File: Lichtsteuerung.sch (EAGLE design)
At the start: 186 parts, among them IC1 74HC595D, IC10 TSR_1-2450, IC11 MEGA64-A, IC12 75176AD, IC13 DS1307SO8, IC2 74HC595D, IC3 74HC595D, IC4 74HC595D, IC5 75176AD, IC6 MEGA8-AI, IC9 24FC128-I/SN, Q1 32.768, Q2 16MHz, Q3 16MHz, U1 MAX232SOIC16, X1 713-1410, X2 713-1410, X3 733-333, X5 713-1410, X6 733-334, X7 733-333, X8 733-333

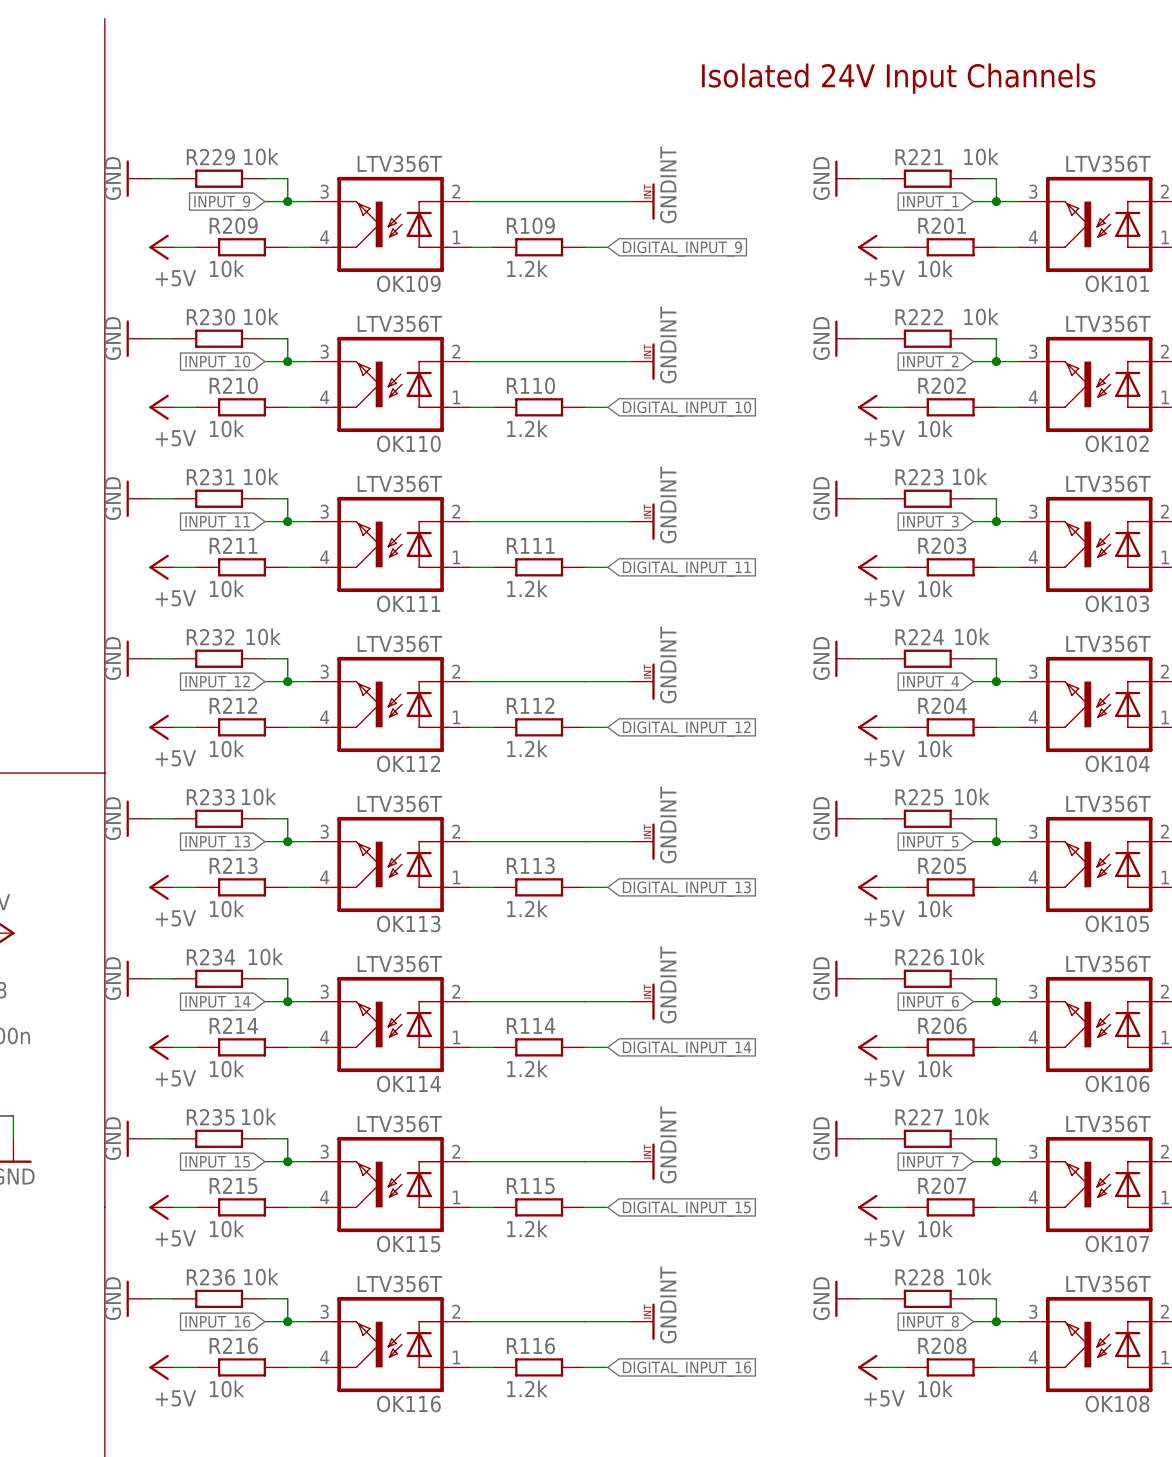
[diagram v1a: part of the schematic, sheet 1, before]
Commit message: Changed pulldown resistors from 10k to 47k for the input optocouplers
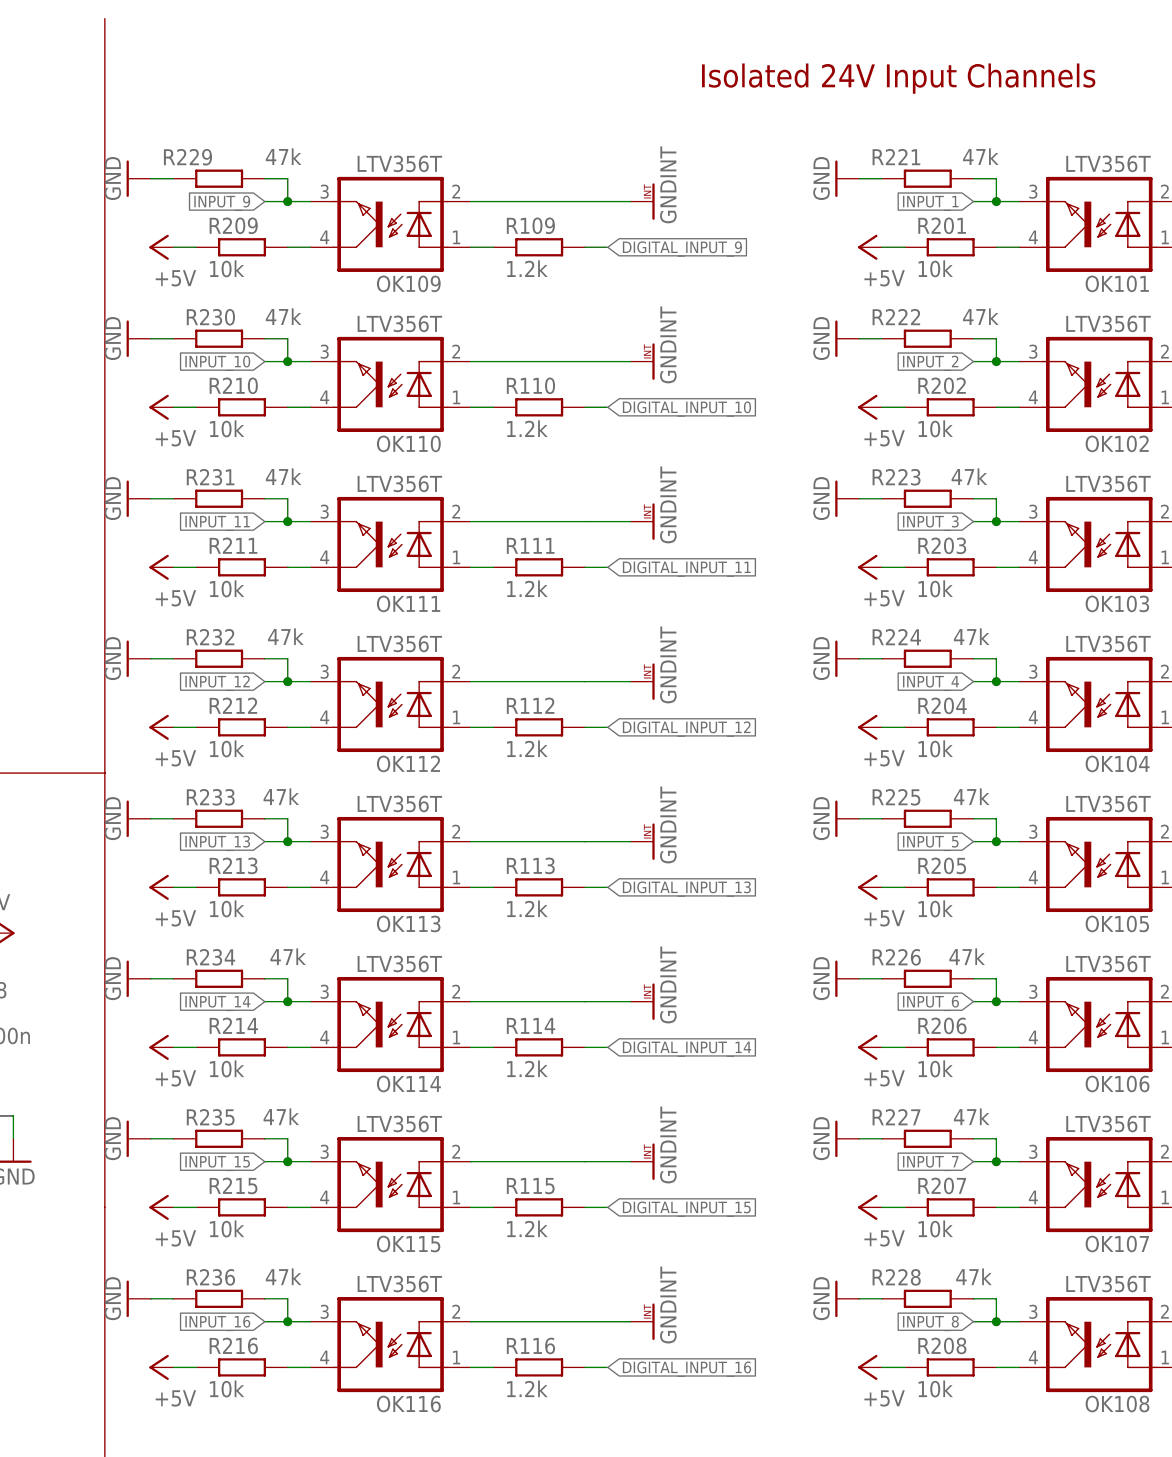
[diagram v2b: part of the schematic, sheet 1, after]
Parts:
- R221, R222, R223, R224, R225, R226, R227, R228, R229, R230, R231, R232, R233, R234, R235, R236: value 10k -> 47k; OC_REICHELT SMD-0805 10,0K -> SMD-0805 47,0K

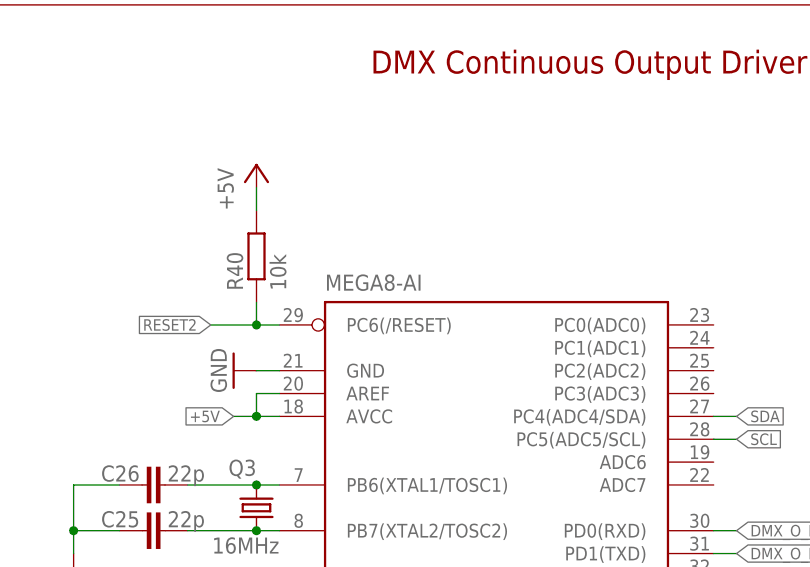
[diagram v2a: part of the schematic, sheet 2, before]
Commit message: Replaced atmega8 with atmega168 in order to use the DMXSerial library
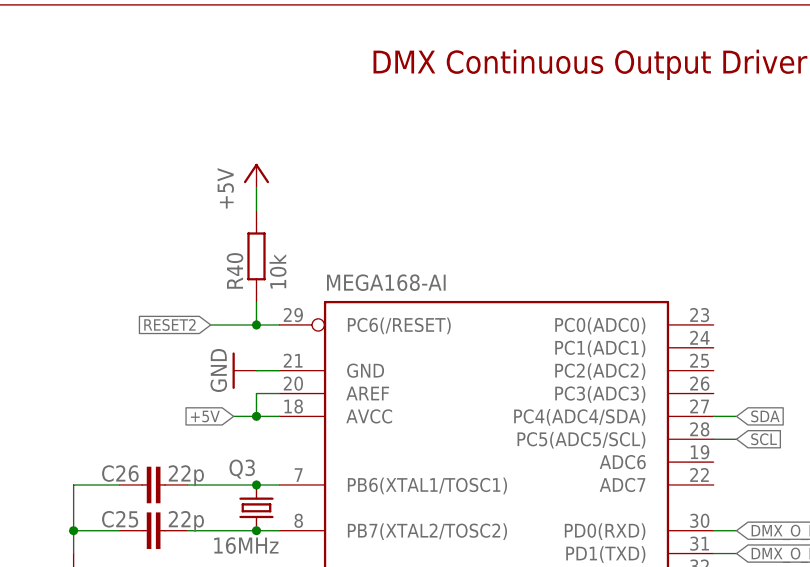
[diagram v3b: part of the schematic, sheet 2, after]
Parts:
- IC6: value MEGA8-AI -> MEGA168-AI; OC_REICHELT ATMEGA 8A-AU -> ATMEGA 168A-AU
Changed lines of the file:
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@@
 <part name="P+17" library="supply1" deviceset="+5V" device=""/>
 <part name="GND29" library="supply1" deviceset="GND" device=""/>
-<part name="IC6" library="atmel" deviceset="MEGA8" device="-AI">
-<attribute name="OC_REICHELT" value="ATMEGA 8A-AU"/>
+<part name="IC6" library="atmel" deviceset="MEGA8" device="-AI" value="MEGA168-AI">
+<attribute name="OC_REICHELT" value="ATMEGA 168A-AU"/>
 </part>
 <part name="R40" library="resistor" deviceset="R-EU_" device="R0805" value="10k">

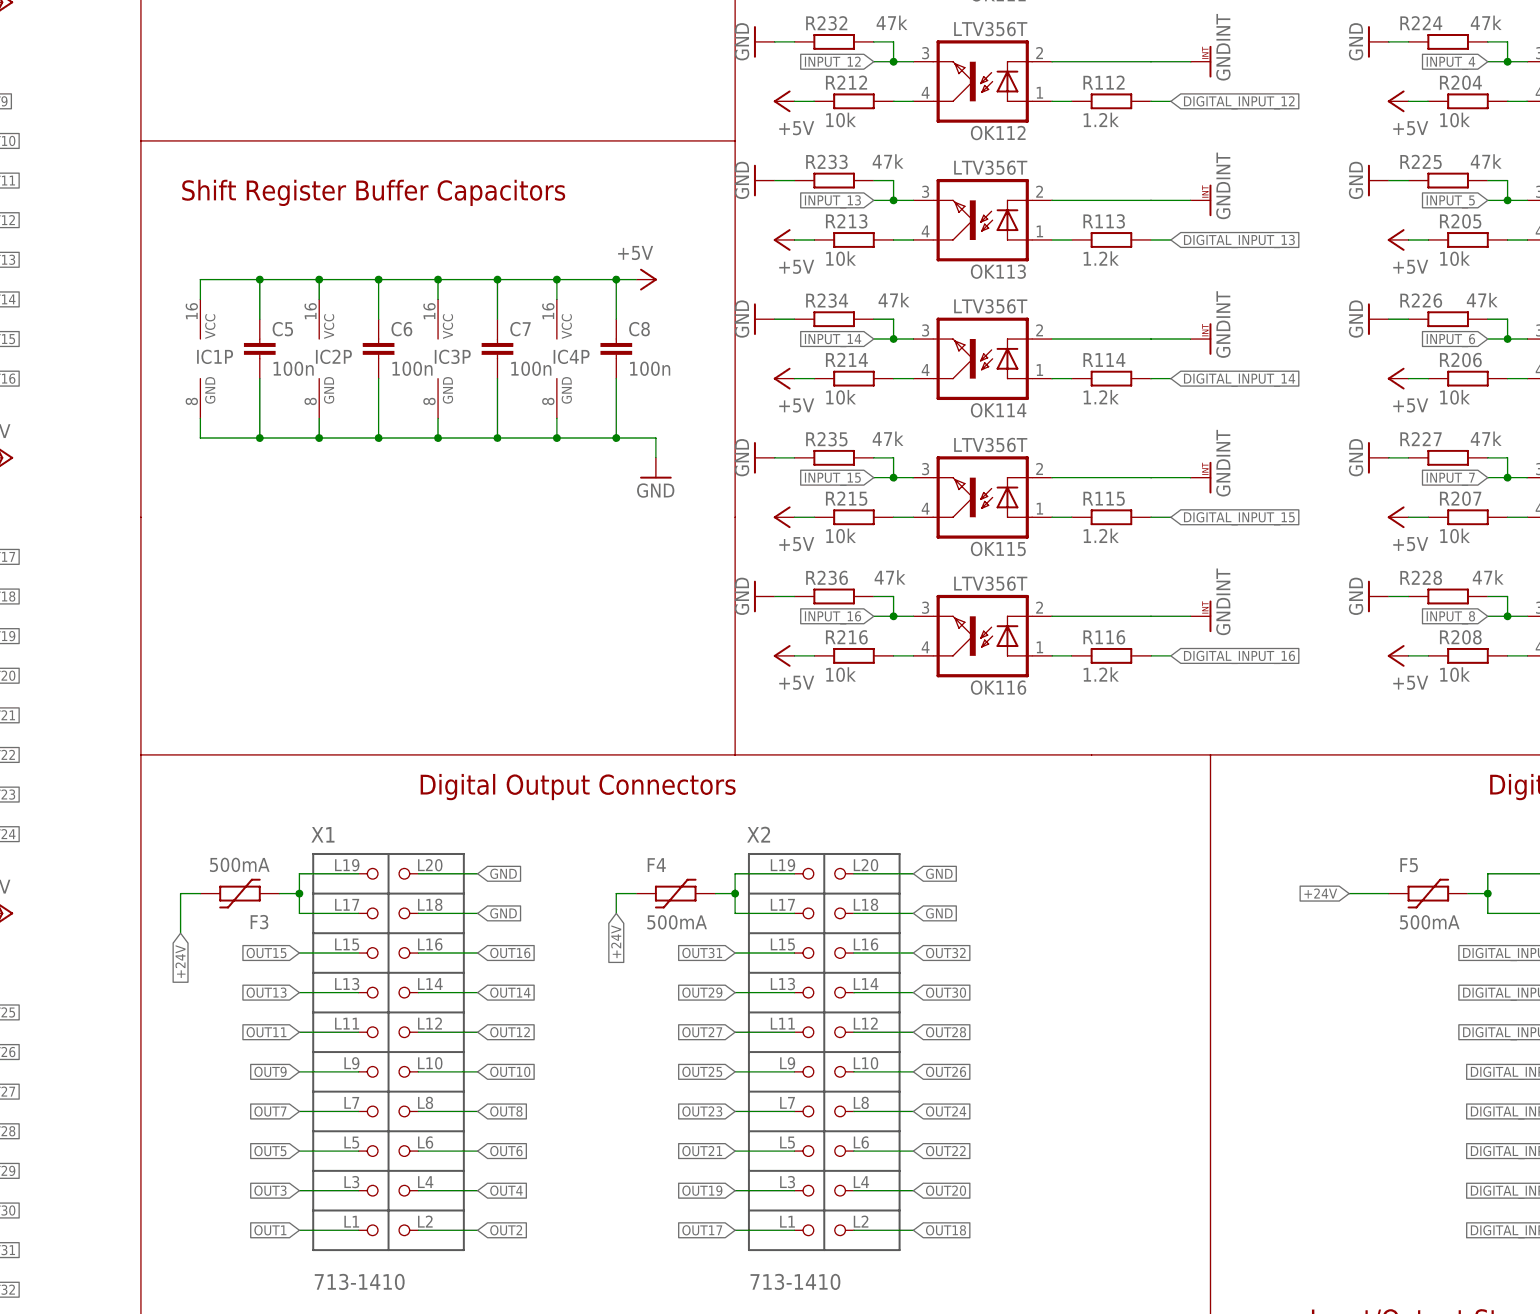
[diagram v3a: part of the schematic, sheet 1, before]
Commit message: Added experimental external power input, needs review from DaFo
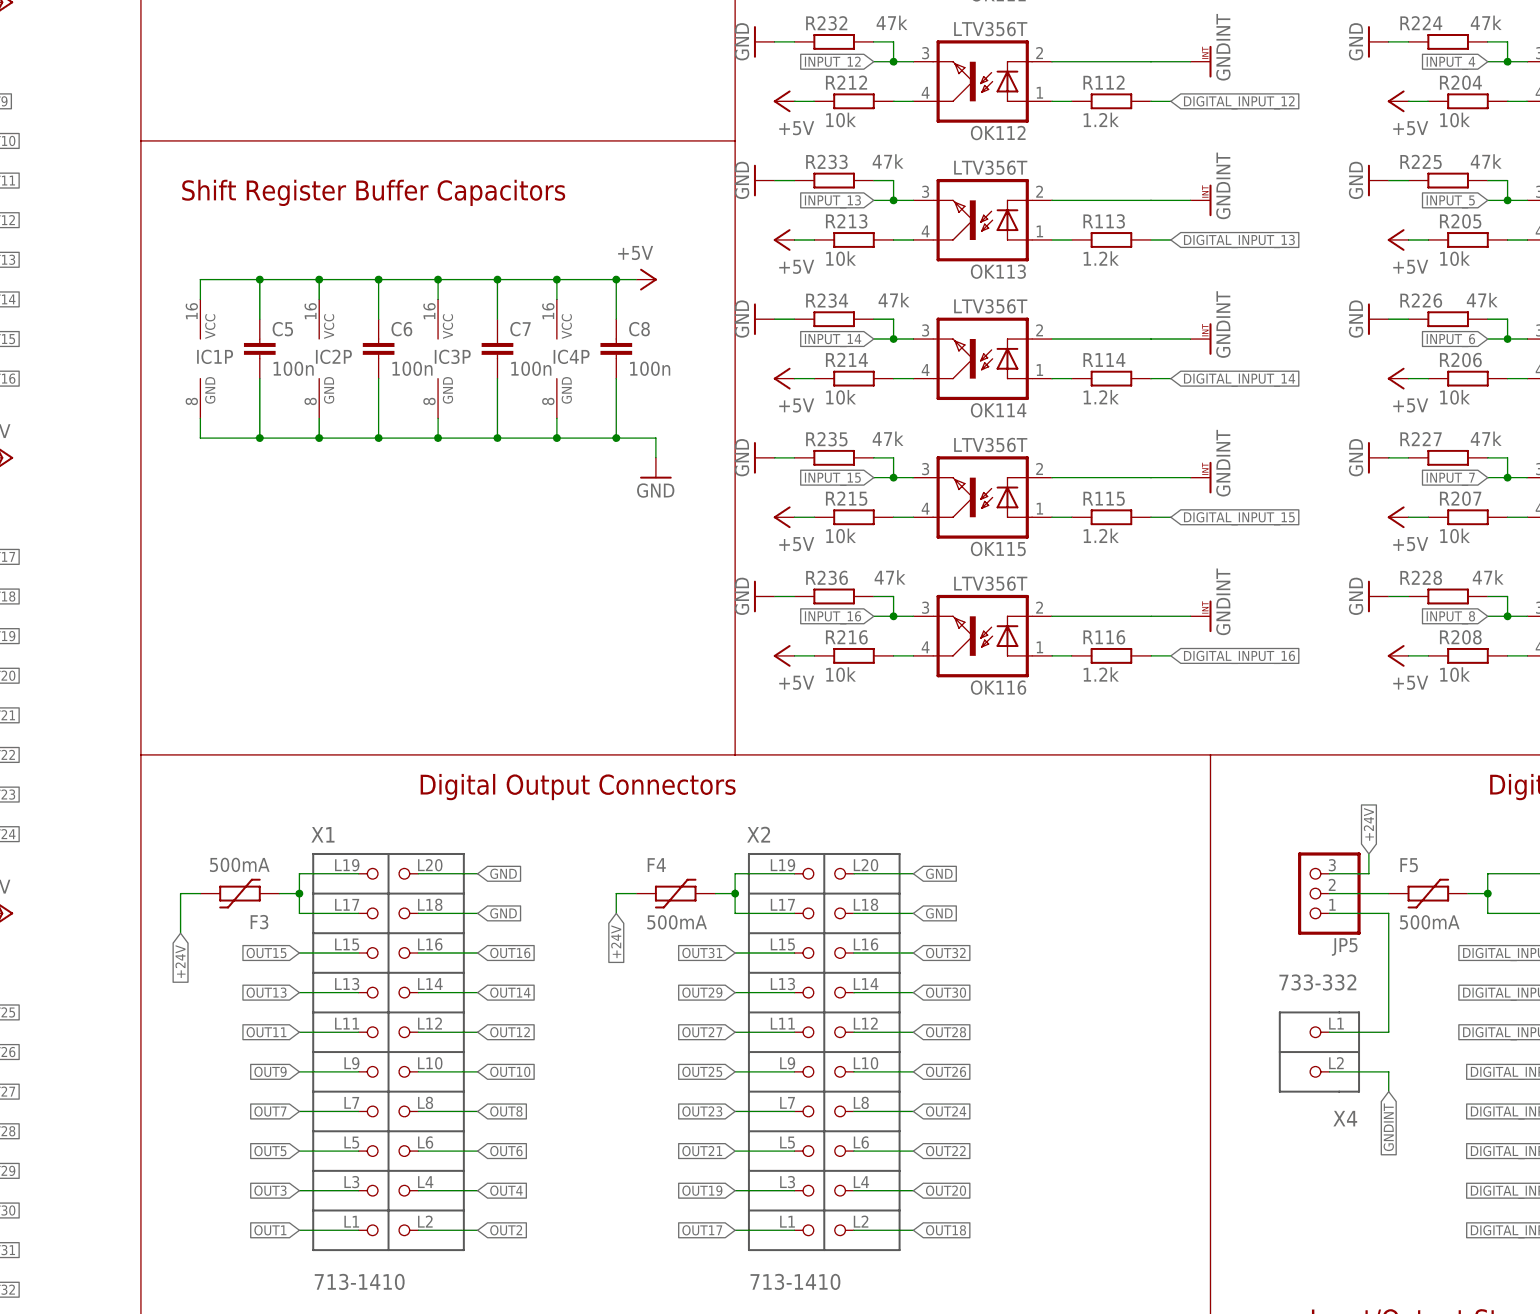
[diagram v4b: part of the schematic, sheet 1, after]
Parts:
- added JP5: (no value), pinhead:PINHD-1X3
- added X4: 733-332, con-wago_2.5mm:733-332
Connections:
- new net N$46: F5.1, JP5.2
- new net N$47: JP5.1, X4.P1
- net +24V: now also JP5.3; no longer F5.1
- net GNDINT: now also X4.P2
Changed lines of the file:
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@@
 <part name="TP5" library="testpad" deviceset="TP" device="PAD1-13"/>
 <part name="TP6" library="testpad" deviceset="TP" device="PAD1-13"/>
+<part name="JP5" library="pinhead" deviceset="PINHD-1X3" device=""/>
+<part name="X4" library="con-wago_2.5mm" deviceset="733-332" device=""/>
 </parts>
 <sheets>
@@
 <wire x1="137.16" y1="256.54" x2="139.7" y2="256.54" width="0.1524" layer="94"/>
 <wire x1="139.7" y1="256.54" x2="139.7" y2="172.72" width="0.1524" layer="94"/>
-<wire x1="139.7" y1="172.72" x2="139.7" y2="124.46" width="0.1524" layer="94"/>
-<wire x1="139.7" y1="124.46" x2="139.7" y2="93.98" width="0.1524" layer="94"/>
+<wire x1="139.7" y1="172.72" x2="139.7" y2="93.98" width="0.1524" layer="94"/>
 <wire x1="139.7" y1="93.98" x2="139.7" y2="5.08" width="0.1524" layer="94"/>
 <wire x1="139.7" y1="172.72" x2="215.9" y2="172.72" width="0.1524" layer="94"/>
 <wire x1="215.9" y1="256.54" x2="215.9" y2="172.72" width="0.1524" layer="94"/>
-<wire x1="215.9" y1="172.72" x2="215.9" y2="124.46" width="0.1524" layer="94"/>
-<wire x1="215.9" y1="124.46" x2="215.9" y2="93.98" width="0.1524" layer="94"/>
+<wire x1="215.9" y1="172.72" x2="215.9" y2="93.98" width="0.1524" layer="94"/>
 <wire x1="139.7" y1="93.98" x2="215.9" y2="93.98" width="0.1524" layer="94"/>
-<wire x1="215.9" y1="93.98" x2="261.62" y2="93.98" width="0.1524" layer="94"/>
+<wire x1="215.9" y1="93.98" x2="276.86" y2="93.98" width="0.1524" layer="94"/>
 <wire x1="276.86" y1="93.98" x2="383.54" y2="93.98" width="0.1524" layer="94"/>
 <wire x1="383.54" y1="93.98" x2="383.54" y2="91.44" width="0.1524" layer="94"/>
-<wire x1="261.62" y1="93.98" x2="276.86" y2="93.98" width="0.1524" layer="94"/>
 <wire x1="276.86" y1="93.98" x2="276.86" y2="5.08" width="0.1524" layer="94"/>
 <text x="344.17" y="20.32" size="2.54" layer="94" font="vector" ratio="7">Felicitus</text>
@@
 <attribute name="VALUE" x="311.15" y="222.504" size="1.778" layer="96"/>
 </instance>
+<instance part="JP5" gate="A" x="289.56" y="76.2" rot="R180"/>
+<instance part="X4" gate="G$1" x="289.56" y="55.88" rot="R180"/>
 </instances>
 <busses>
@@
 </segment>
 <segment>
-<pinref part="F5" gate="G$1" pin="1"/>
-<wire x1="299.72" y1="76.2" x2="294.64" y2="76.2" width="0.1524" layer="91"/>
-<label x="294.64" y="76.2" size="1.27" layer="95" rot="R180" xref="yes"/>
-</segment>
-<segment>
 <pinref part="F4" gate="G$1" pin="1"/>
 <wire x1="203.2" y1="76.2" x2="200.66" y2="76.2" width="0.1524" layer="91"/>
@@
 <wire x1="144.78" y1="76.2" x2="144.78" y2="71.12" width="0.1524" layer="91"/>
 <label x="144.78" y="71.12" size="1.27" layer="95" rot="R270" xref="yes"/>
+</segment>
+<segment>
+<pinref part="JP5" gate="A" pin="3"/>
+<wire x1="292.1" y1="78.74" x2="297.18" y2="78.74" width="0.1524" layer="91"/>
+<wire x1="297.18" y1="78.74" x2="297.18" y2="81.28" width="0.1524" layer="91"/>
+<label x="297.18" y="81.28" size="1.27" layer="95" rot="R90" xref="yes"/>
 </segment>
 </net>
@@
 <label x="347.98" y="73.66" size="1.27" layer="95" xref="yes"/>
 <pinref part="X5" gate="G$1" pin="L18"/>
+</segment>
+<segment>
+<pinref part="X4" gate="G$1" pin="P2"/>
+<wire x1="292.1" y1="53.34" x2="299.72" y2="53.34" width="0.1524" layer="91"/>
+<wire x1="299.72" y1="53.34" x2="299.72" y2="50.8" width="0.1524" layer="91"/>
+<label x="299.72" y="50.8" size="1.27" layer="95" rot="R270" xref="yes"/>
 </segment>
 </net>
@@
 </segment>
 </net>
+<net name="N$46" class="0">
+<segment>
+<pinref part="F5" gate="G$1" pin="1"/>
+<pinref part="JP5" gate="A" pin="2"/>
+<wire x1="299.72" y1="76.2" x2="292.1" y2="76.2" width="0.1524" layer="91"/>
+</segment>
+</net>
+<net name="N$47" class="0">
+<segment>
+<pinref part="X4" gate="G$1" pin="P1"/>
+<wire x1="292.1" y1="58.42" x2="299.72" y2="58.42" width="0.1524" layer="91"/>
+<wire x1="299.72" y1="58.42" x2="299.72" y2="73.66" width="0.1524" layer="91"/>
+<pinref part="JP5" gate="A" pin="1"/>
+<wire x1="299.72" y1="73.66" x2="292.1" y2="73.66" width="0.1524" layer="91"/>
+</segment>
+</net>
